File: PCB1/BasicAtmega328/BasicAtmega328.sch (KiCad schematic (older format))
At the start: 16 parts

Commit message: Arduino terminado y alimentacion
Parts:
- added C? (x2): 47uF, symbol device:CP_Small
- added C?: 100nF, symbol device:C_Small
- added D?: POWER_ON, symbol device:LED_Small_ALT
- added J?: Jack-DC-IN, symbol Connector:Jack-DC
- added JP?: VCC_CUT, symbol device:Jumper_NO_Small
- added P?: SERIAL_DEBUG, symbol conn:CONN_01X04
- added P?: MODBUS_1, symbol conn:CONN_02X03
- added P?: MODBUS_2, symbol conn:CONN_02X03
- added R?: 1k, symbol device:R_Small
- added R? (x3): 10k, symbol device:R_Small
- added R?: 120R(NC), symbol device:R_Small
- added U?: LM1117-5.0, symbol regul:LM1117-5.0
- D? (x3): value D_TVS -> SMBJ6.0CA
- P?: value CONN_01X15 -> HEADER2
- P?: value CONN_01X15 -> HEADER1
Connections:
- net +5V: now also P?.4 (P4), U?.8 (VCC), C?.1, C?.1, JP?.1, R?.1, R?.1, R?.2, U?.2 (VO)
- net A0: now also P?.12 (P12)
- net A1: now also P?.11 (P11)
- net A2: now also P?.10 (P10)
- net A3: now also P?.9 (P9)
- net A4: now also P?.8 (P8)
- net A5: now also P?.7 (P7)
- net A6: now also P?.6 (P6)
- net A7: now also P?.5 (P5)
- net D10: now also P?.13 (P13)
- net D11-MOSI: now also P?.14 (P14)
- net D12-MISO: now also P?.15 (P15)
- net D13-SCK: now also P?.15 (P15)
- net D2: now also P?.5 (P5)
- net D3: now also P?.6 (P6)
- net D4: now also P?.7 (P7)
- net D5: now also P?.8 (P8)
- net D6: now also P?.9 (P9)
- net D7: now also P?.10 (P10)
- net D8: now also P?.11 (P11)
- net D9: now also P?.12 (P12)
- net GND: now also P?.2 (P2), P?.4 (P4), U?.5 (GND), C?.2, C?.2, C?.2, D?.1 (K), J?.2, J?.3, P?.2 (P2), P?.2 (P2), P?.4 (P4), R?.2, U?.1 (GND)
- net RST: now also P?.3 (P3), P?.3 (P3)
- net AREF: now reaches C?.1, U?.20 (AREF)
- net AREF: now also P?.13 (P13)
- net +12V: now reaches P?.1 (P1)
- net +12V: now also C?.1, J?.1, P?.1 (P1), P?.1 (P1), U?.3 (VI)
- net DO: now reaches U?.1 (RO)
- net at U?.2 (~RE): now also U?.3 (~SHDN), R?.1
- net DI: now reaches U?.4 (DI)
- net at D?.1 (A1), D?.2 (A2), F?.2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: now also R?.1, R?.2
- net at D?.1 (A1), D?.2 (A2), F?.1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: now also R?.1, R?.2
- net B-: now reaches F?.2
- net B-: now also P?.4 (P4), P?.4 (P4)
- net A+: now reaches F?.1
- net A+: now also P?.3 (P3), P?.3 (P3)
- new net: JP?.2, P?.1 (P1)
- new net: D?.2 (A), R?.2
- new net: P?.5 (P5), P?.5 (P5)
- new net: P?.6 (P6), P?.6 (P6)
- no-connect marks 0 -> 1
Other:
- moved on the sheet: P?

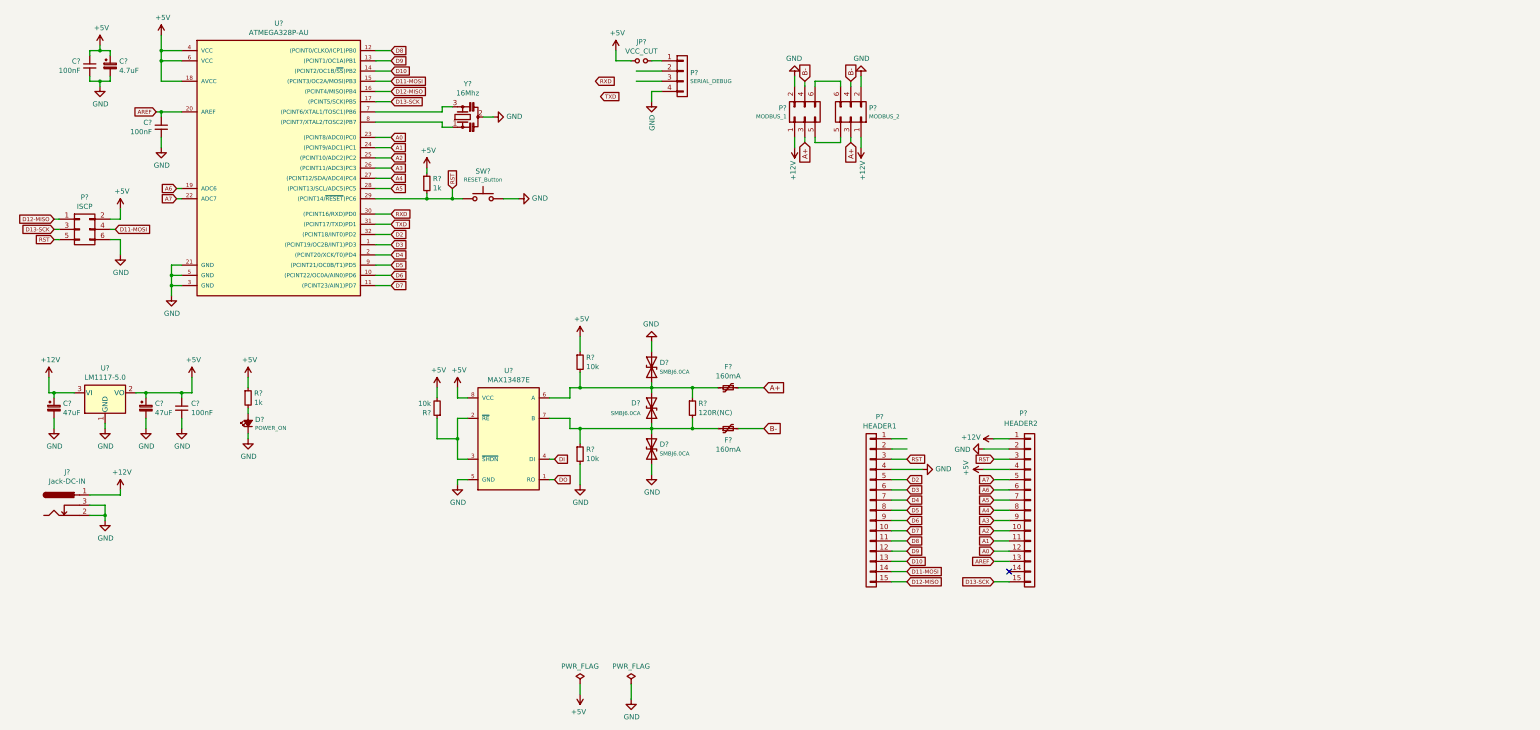
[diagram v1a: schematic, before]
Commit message: Faltan uarts y validacion
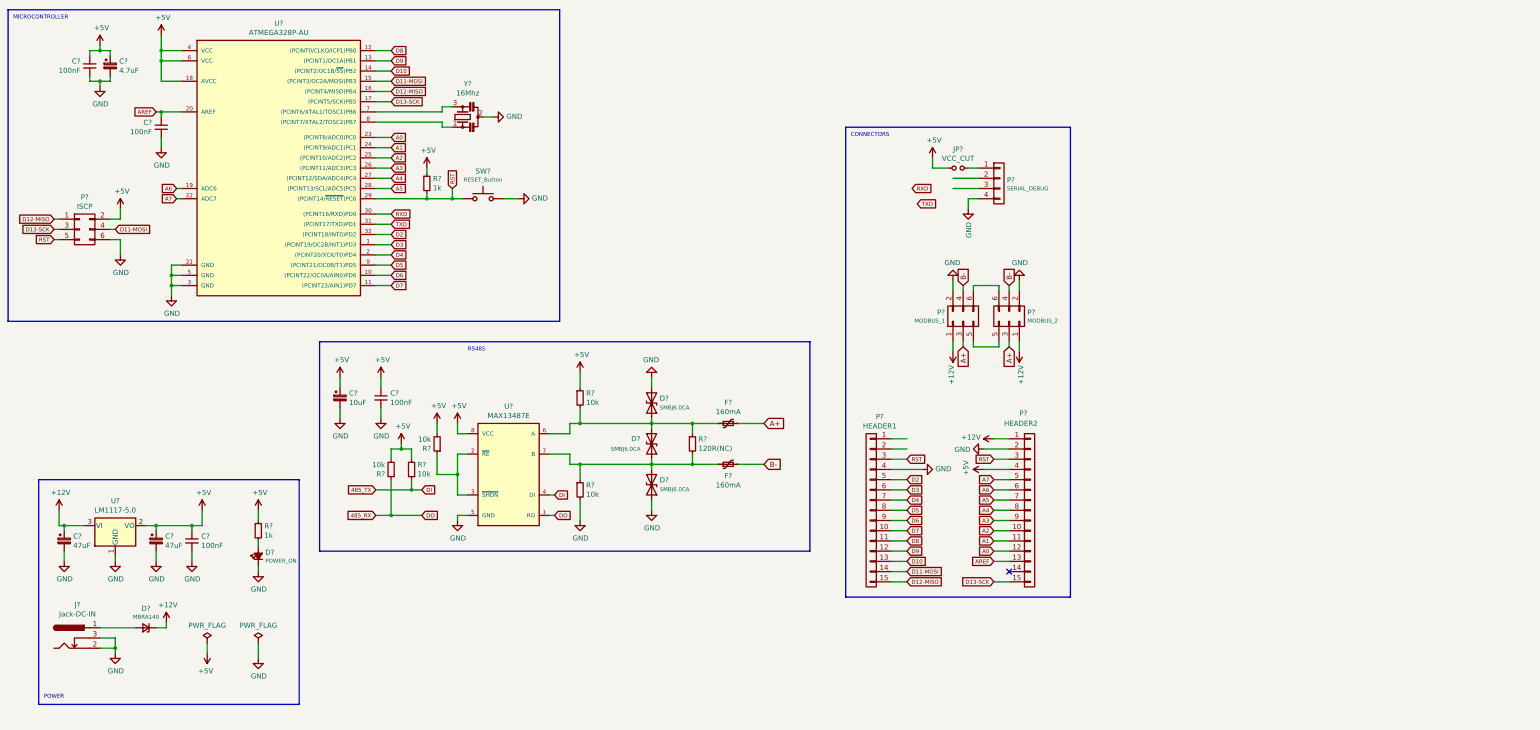
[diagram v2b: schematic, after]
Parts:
- added C?: 10uF, symbol device:CP_Small
- added C?: 100nF, symbol device:C_Small
- added D?: MBRA140, symbol device:D_Zener_Small
- added R? (x2): 10k, symbol device:R_Small
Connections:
- net +12V: now also D?.1 (K); no longer J?.1
- net +5V: now also C?.1, C?.1, R?.2, R?.2
- net GND: now also C?.2, C?.2
- net DI renamed 485_TX
- net 485_TX: now also R?.1
- net DO renamed 485_RX
- net 485_RX: now also R?.1
- new net: D?.2 (A), J?.1
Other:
- note added: "CONNECTORS"
- note added: "MICROCONTROLLER"
- note added: "POWER\n"
- note added: "RS485"
- moved on the sheet: C?, D?, F?, J?, JP?, P?, R?, U?

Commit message: Cvpcb terminado
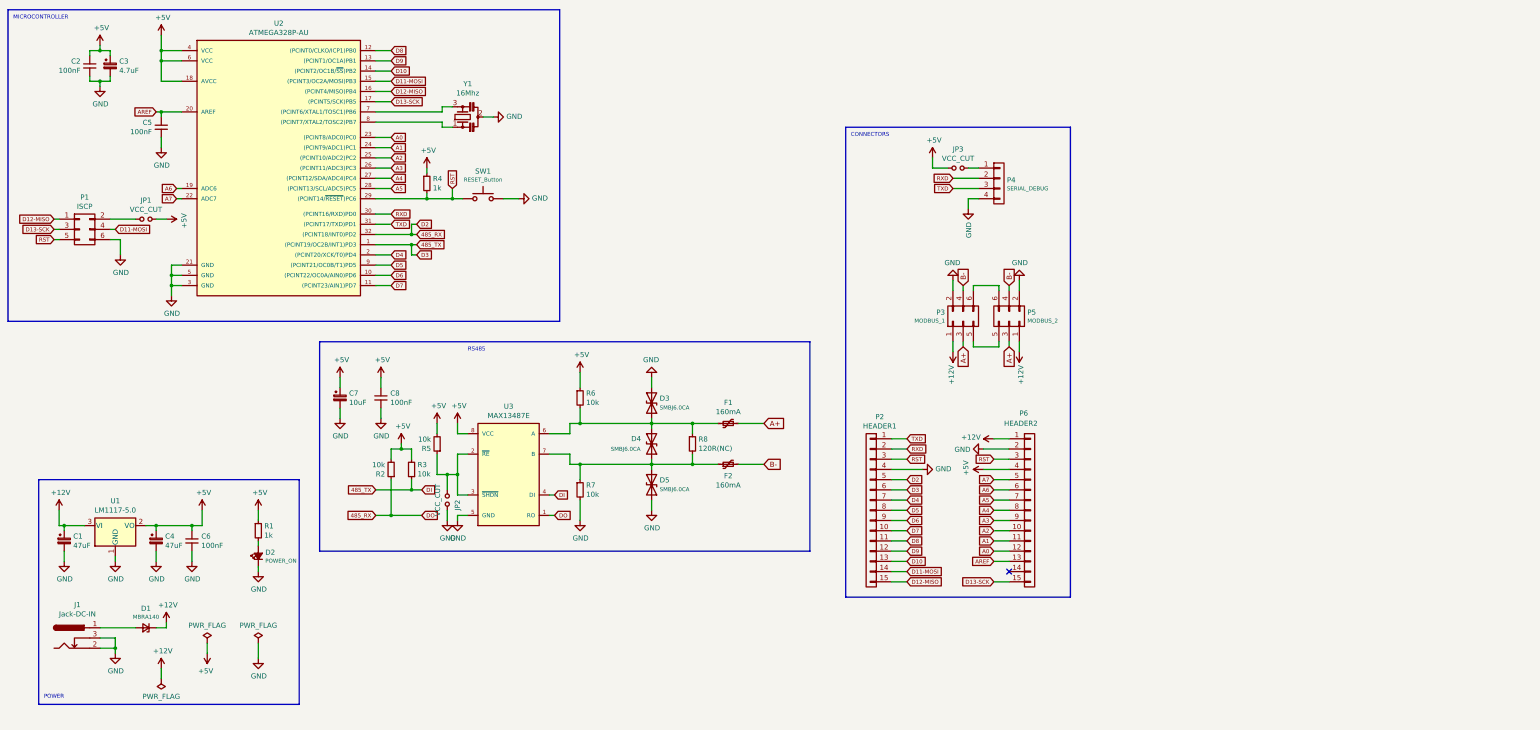
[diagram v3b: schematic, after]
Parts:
- added JP1, JP2: VCC_CUT, Jumpers:SMT-JUMPER_2_NO_NO-SILK, symbol device:Jumper_NO_Small
- C1, C4: renamed from C?; footprint (none) -> Capacitors_SMD:CP_Elec_6.3x5.7
- C2, C3, C5, C6, C7, C8: renamed from C?; footprint (none) -> Capacitors_SMD:C_0805
- D1: renamed from D?; footprint (none) -> Diodes_SMD:D_SMA_Standard
- D2: renamed from D?; footprint (none) -> LEDs:LED_0805
- D3, D4, D5: renamed from D?; footprint (none) -> Diode_SMD:D_SMB
- F1, F2: renamed from F?; footprint (none) -> Fuses:1206
- J1: renamed from J?; footprint (none) -> Connectors:BARREL_JACK
- JP3: renamed from JP?; footprint (none) -> Jumpers:SMT-JUMPER_2_NO_NO-SILK
- P1: renamed from P?; footprint (none) -> Connectors:2X3
- P2, P5: renamed from P?; footprint (none) -> Pin_Headers:Pin_Header_Straight_1x15
- P3, P6: renamed from P?; footprint (none) -> Connectors_Molex:Molex_Microfit3_Header_02x03_Angled_43045-060x
- P4: renamed from P?; footprint (none) -> Connectors_JST:JST_PH_S4B-PH-K_04x2.00mm_Angled
- R1, R2, R3, R4, R5, R6, R7, R8: renamed from R?; footprint (none) -> Resistors_SMD:R_0805
- SW1: renamed from SW?; footprint (none) -> Buttons_Switches_SMD:SW_SPST_B3U-3000P
- U1: renamed from U?; footprint (none) -> TO_SOT_Packages_SMD:SOT-223-3_TabPin2
- U3: renamed from U?; footprint SO08 -> Housings_SOIC:SO-8_5.3x6.2mm_Pitch1.27mm
- Y1: renamed from Y?; footprint (none) -> Clocks:RESONATOR-SMD-3.2X1.3
- gave numbers to parts that had none: 1
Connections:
- net D2 is gone; now on net 485_RX: P2.5 (P5), U2.32 ((PCINT18/INT0)PD2)
- net D3 is gone; now on net 485_TX: P2.6 (P6), U2.1 ((PCINT19/OC2B/INT1)PD3)
- net +5V: now also JP1.2; no longer P1.2 (P2)
- net GND: now also JP2.1
- net RXD: now also P2.2 (P2), P4.2 (P2)
- net TXD: now also P2.1 (P1), P4.3 (P3)
- net at R5.1, U3.2 (~RE), U3.3 (~SHDN): now also JP2.2
- new net: JP1.1, P1.2 (P2)

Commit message: Placa enrutada
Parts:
- removed C4: 47uF, Capacitors_SMD:CP_Elec_6.3x5.7, symbol device:CP_Small
- P5: footprint Pin_Headers:Pin_Header_Straight_1x15 -> Connectors_Molex:Molex_Microfit3_Header_02x03_Angled_43045-060x
- P6: footprint Connectors_Molex:Molex_Microfit3_Header_02x03_Angled_43045-060x -> Pin_Headers:Pin_Header_Straight_1x15
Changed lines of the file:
@@
 F 0 "P6" H 10500 6500 50  0000 L CNN
 F 1 "HEADER2" H 10350 6400 50  0000 L CNN
-F 2 "Connectors_Molex:Molex_Microfit3_Header_02x03_Angled_43045-060x" H 10600 5550 50  0001 C CNN
+F 2 "Pin_Headers:Pin_Header_Straight_1x15" H 10600 5550 50  0001 C CNN
 F 3 "" H 10600 5550 50  0001 C CNN
 	1    10600 5550
@@
 	1650 6000 1650 6050
 Wire Wire Line
-	1950 5700 2050 5700
-Wire Wire Line
 	2500 5700 2500 5550
 $Comp
@@
 $EndComp
 $Comp
-L device:CP_Small C4
-U 1 1 5FEFBF30
-P 2050 5850
-F 0 "C4" H 2138 5896 50  0000 L CNN
-F 1 "47uF" H 2138 5805 50  0000 L CNN
-F 2 "Capacitors_SMD:CP_Elec_6.3x5.7" H 2050 5850 50  0001 C CNN
-F 3 "" H 2050 5850 50  0001 C CNN
-	1    2050 5850
-	1    0    0    -1
-$EndComp
-$Comp
 L device:C_Small C6
 U 1 1 5FEFC93E
@@
 $EndComp
 Wire Wire Line
-	2050 5750 2050 5700
-Connection ~ 2050 5700
-Wire Wire Line
 	2400 5700 2400 5750
-Wire Wire Line
-	2050 5700 2400 5700
 Wire Wire Line
 	2400 5700 2500 5700
@@
 $EndComp
 $Comp
-L CH340G_D-SUN-V3.0-cache:GND #PWR0121
-U 1 1 5FF12DA4
-P 2050 6050
-F 0 "#PWR0121" H 2050 5800 50  0001 C CNN
-F 1 "GND" H 2055 5877 50  0000 C CNN
-F 2 "" H 2050 6050 60  0000 C CNN
-F 3 "" H 2050 6050 60  0000 C CNN
-	1    2050 6050
-	1    0    0    -1
-$EndComp
-$Comp
 L CH340G_D-SUN-V3.0-cache:GND #PWR0122
 U 1 1 5FF12F5E
@@
 Wire Wire Line
 	2400 5950 2400 6050
-Wire Wire Line
-	2050 5950 2050 6050
 Wire Wire Line
 	1150 5950 1150 6050
@@
 F 0 "P5" V 10438 3828 50  0000 L CNN
 F 1 "MODBUS_2" V 10355 3828 39  0000 L CNN
-F 2 "Pin_Headers:Pin_Header_Straight_1x15" H 10400 2450 50  0001 C CNN
+F 2 "Connectors_Molex:Molex_Microfit3_Header_02x03_Angled_43045-060x" H 10400 2450 50  0001 C CNN
 F 3 "" H 10400 2450 50  0001 C CNN
 	1    10400 3650
@@
 Wire Wire Line
 	2100 7100 2100 7200
+Wire Wire Line
+	1950 5700 2400 5700
 $EndSCHEMATC
